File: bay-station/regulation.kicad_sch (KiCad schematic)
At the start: 7 parts, among them U8 TPS62A02PDDCR

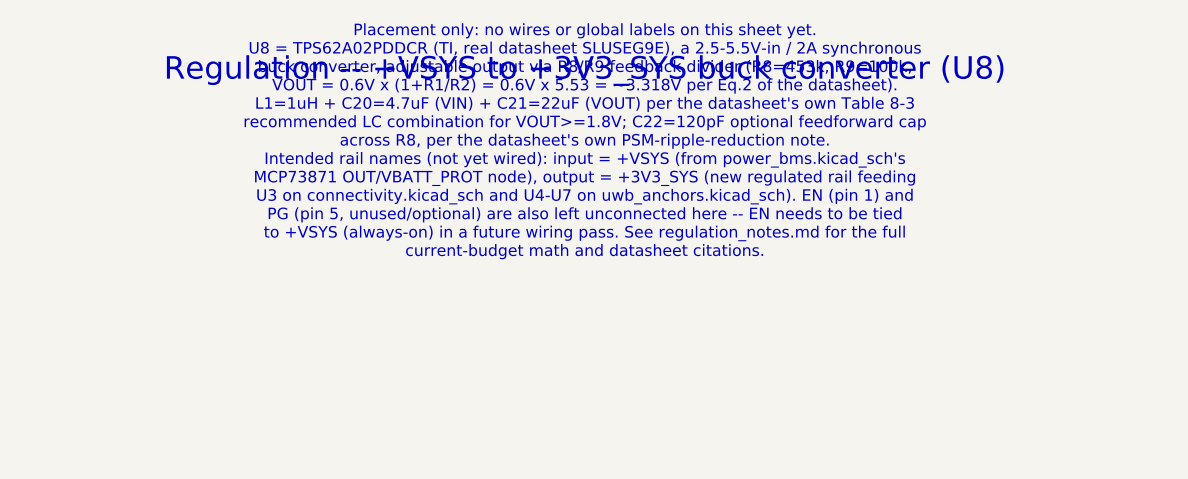
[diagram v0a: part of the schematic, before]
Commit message: Bay station: discrete DW3210 array on a shared clock, Nordic BT840 host
Two coupled changes, both forced by the positioning scheme.

UWB ARRAY. TDoA compares timestamps across receivers, so they must share a
time base. The DWM3000 module makes that impossible -- its 24 pins contain
no clock pin and its crystal is internal and unreachable, so four of them
cannot be synchronised at any price. The bare DW3000 IC can: Datasheet v1.3
Table 10 states a 38.4 MHz signal may be supplied from an external reference
via the XTI overdrive pin. Four DW3210s (QFN40, not the 52-ball WLCSP
DW3110 the module is built on) now sit on one PCB sharing one TCXO through
a 1:4 low-skew buffer, with the antennas remote on ~1-2 m SMA coax. This
makes synchronisation structurally absent rather than solved.

uwb_anchors.kicad_sch renamed to uwb_array.kicad_sch -- the four receivers
are one on-board array, not distributed anchor units. U4 is A0, the CENTER
anchor; U5-U7 are A1-A3 outer. They are not interchangeable peers.

New clock_dist.kicad_sch holds the shared reference network. Placed are only
the passives the datasheet actually specifies: 2200 pF AC coupling into each
XTI and 1 pF from each XTO to ground, both required only because an external
clock is used. TCXO and buffer parts are not yet selected.

HOST MCU. The uplink moved from WiFi-to-internet to BLE-to-a-laptop, and
WiFi was the only thing keeping this board off Nordic. ESP32-S3-WROOM-1 is
replaced by a Fanstel BT840 (nRF52840), which gives one toolchain across
both boards and aligns with Qorvo's DW3000 reference stack -- easing the
multi-instance driver work that sits on the critical path. Note the
ESP32-S3 is BLE-only with no Classic/SPP, so the laptop link is a GATT
service.

programming_debug collapsed accordingly: Nordic programs over SWD, so the
boot straps, EN RC delay, BOOT button and the data-capable USB-C are gone,
replaced by a 2x5 ARM Cortex Debug header. That RESOLVES the long-standing
two-USB-C open item by deletion -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
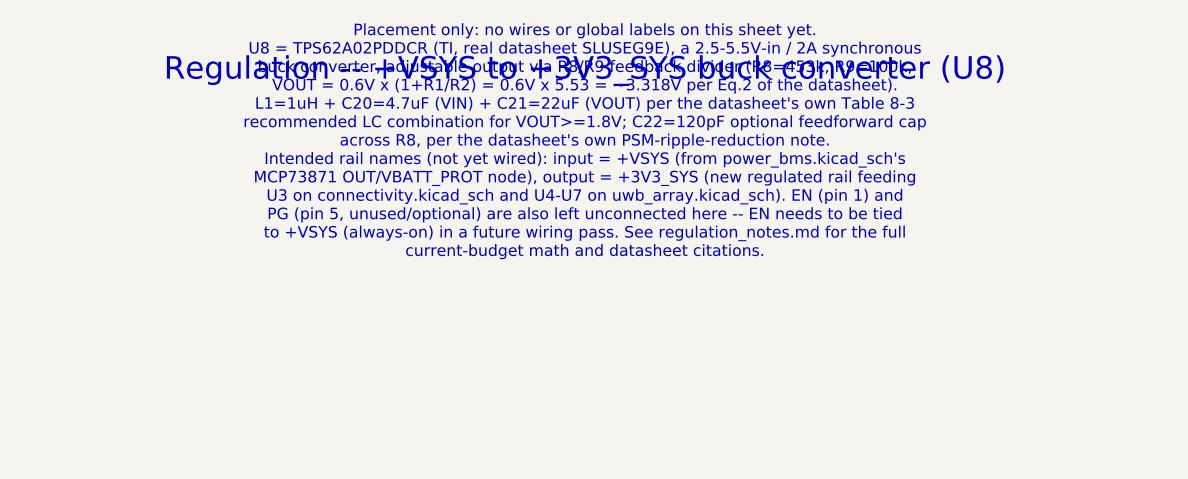
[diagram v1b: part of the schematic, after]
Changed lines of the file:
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@@
 	(title_block
 		(title "Regulation")
-		(comment 1 "Bay station -- +VSYS to +3V3_SYS buck regulation (TPS62A02PDDCR) for ESP32-S3 + 4x DWM3000 loads. Placement only -- no wires/labels yet.")
+		(comment 1 "Bay station -- +VSYS to +3V3_SYS buck regulation (TPS62A02PDDCR) for BT840 host + 4x DW3210 anchor loads. Placement only -- no wires/labels yet. Budget re-run 2026-09-19: ~347mA vs 2A rating.")
 	)
 	(text "Regulation -- +VSYS to +3V3_SYS buck converter (U8)"
@@
 		)
 	)
-	(text "Placement only: no wires or global labels on this sheet yet.\nU8 = TPS62A02PDDCR (TI, real datasheet SLUSEG9E), a 2.5-5.5V-in / 2A synchronous\nbuck converter, adjustable output via R8/R9 feedback divider (R8=453k, R9=100k,\nVOUT = 0.6V x (1+R1/R2) = 0.6V x 5.53 = ~3.318V per Eq.2 of the datasheet).\nL1=1uH + C20=4.7uF (VIN) + C21=22uF (VOUT) per the datasheet's own Table 8-3\nrecommended LC combination for VOUT>=1.8V; C22=120pF optional feedforward cap\nacross R8, per the datasheet's own PSM-ripple-reduction note.\nIntended rail names (not yet wired): input = +VSYS (from power_bms.kicad_sch's\nMCP73871 OUT/VBATT_PROT node), output = +3V3_SYS (new regulated rail feeding\nU3 on connectivity.kicad_sch and U4-U7 on uwb_anchors.kicad_sch). EN (pin 1) and\nPG (pin 5, unused/optional) are also left unconnected here -- EN needs to be tied\nto +VSYS (always-on) in a future wiring pass. See regulation_notes.md for the full\ncurrent-budget math and datasheet citations."
+	(text "Placement only: no wires or global labels on this sheet yet.\nU8 = TPS62A02PDDCR (TI, real datasheet SLUSEG9E), a 2.5-5.5V-in / 2A synchronous\nbuck converter, adjustable output via R8/R9 feedback divider (R8=453k, R9=100k,\nVOUT = 0.6V x (1+R1/R2) = 0.6V x 5.53 = ~3.318V per Eq.2 of the datasheet).\nL1=1uH + C20=4.7uF (VIN) + C21=22uF (VOUT) per the datasheet's own Table 8-3\nrecommended LC combination for VOUT>=1.8V; C22=120pF optional feedforward cap\nacross R8, per the datasheet's own PSM-ripple-reduction note.\nIntended rail names (not yet wired): input = +VSYS (from power_bms.kicad_sch's\nMCP73871 OUT/VBATT_PROT node), output = +3V3_SYS (new regulated rail feeding\nU3 on connectivity.kicad_sch and U4-U7 on uwb_array.kicad_sch). EN (pin 1) and\nPG (pin 5, unused/optional) are also left unconnected here -- EN needs to be tied\nto +VSYS (always-on) in a future wiring pass. See regulation_notes.md for the full\ncurrent-budget math and datasheet citations."
 		(at 60 38 0)
 		(effects
